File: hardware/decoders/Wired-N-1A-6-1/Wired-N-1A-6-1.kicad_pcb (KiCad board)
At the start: 2 copper layers, 9 x 25 mm, 53 parts, among them J0 CA, J1 CA, J10 RL, J11 RR, J12 FOF, J13 F0R, J14 MCLR, J15 +5, J16 GND, J17 PGD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

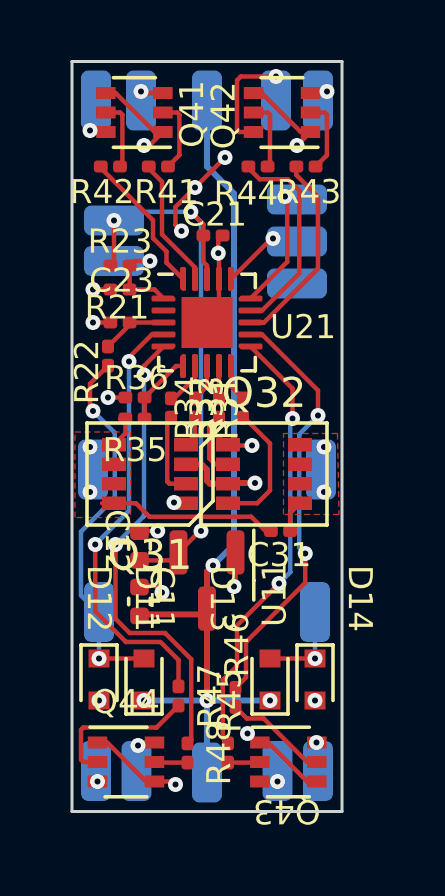
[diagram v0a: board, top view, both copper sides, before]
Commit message: Made Wired-N-1A-6-1 prettier, and easier to follow.
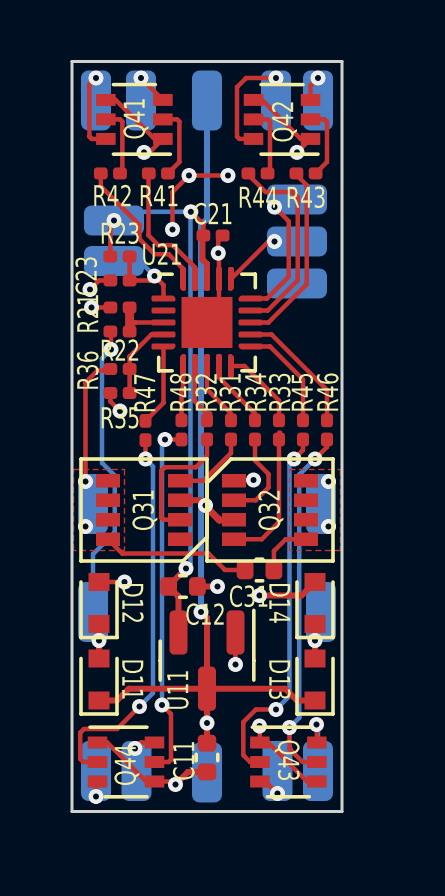
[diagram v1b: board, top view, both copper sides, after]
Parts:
- C11, C12: value 1uF -> 2.2uF
- C31: footprint Capacitor_SMD:C_0201_0603Metric -> Capacitor_SMD:C_0402_1005Metric
- U11: value LR8341A-T50 -> LR8341A
- U21: value PIC18F06Q40 -> PIC18F
- moved R45 11.1 mm to (57.7, 62.3)
- moved R48 10.8 mm to (53.6, 62.3)
- moved R46 9.43 mm to (58.5, 62.3)
- moved R47 8.92 mm to (52.5, 62.3)
- moved C11 5.67 mm to (54.5, 73.2), turned to -90 degrees
- moved U11 2.67 mm to (54.5, 70.0)
- moved D12 2.55 mm to (50.9, 68.0), turned to 90 degrees
- moved D14 2.55 mm to (58.1, 68.0), turned to 90 degrees
- moved C12 1.98 mm to (53.7, 67.5), turned to 0 degrees
- moved R35 1.72 mm to (51.6, 60.2)
- moved D11 1.50 mm to (50.9, 70.6)
- moved D13 1.50 mm to (58.1, 70.6)
- moved C31 1.48 mm to (56.2, 67.0)
- moved R32 1.40 mm to (54.5, 62.3)
- moved R34 1.40 mm to (56.1, 62.3)
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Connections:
- U21 pad 4: F6 -> BackEMF
- U21 pad 5: F0R -> F6
- U21 pad 6: BackEMF -> F0R
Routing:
- net F0R: track 15.7 -> 1.60 mm, vias 2 -> 0
- net F6: track 14.7 -> 2.73 mm, vias 2 -> 0
- net F4: track 14.9 -> 3.34 mm, vias 2 -> 0
- net Net-(Q43-Pad2): track 1.07 -> 12.4 mm, vias 0 -> 2
- net Net-(Q44-Pad5): track 1.11 -> 12.1 mm, vias 0 -> 2
- net F5: track 14.2 -> 4.10 mm, vias 2 -> 0
- net Net-(Q43-Pad5): track 3.47 -> 11.9 mm, vias 0 -> 2
- net Net-(Q44-Pad2): track 5.16 -> 13.0 mm, vias 0 -> 2
- net GND: track 24.1 -> 27.3 mm, vias 18 -> 16
- net FOF_SP: track 0.00 -> 2.63 mm
- net F4_SP: track 0.00 -> 2.18 mm
- net MOT_A: track 7.23 -> 9.29 mm
- net Net-(Q31-Pad2): track 2.84 -> 4.49 mm
- net Net-(Q31-Pad4): track 1.03 -> 2.53 mm
- net +5V: track 19.9 -> 21.2 mm
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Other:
- board text added: "Wired-N-1A-6-1"

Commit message: Bring inline with Breadboard-1 reference design.
Add digital transitor drivers for the high side of the H-Bridge.
Add third BEMF resistor.
Relocate noise capacitor.
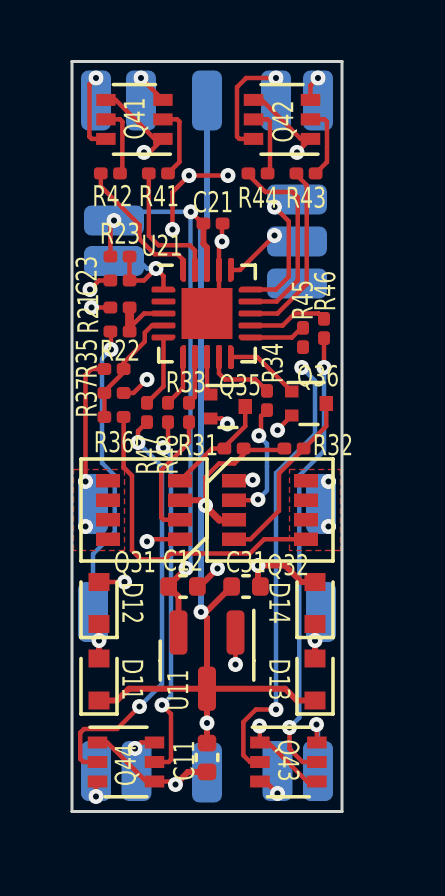
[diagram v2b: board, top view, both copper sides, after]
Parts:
- added Q35: DTC143Z, Package_TO_SOT_SMD:SOT-723, F.Cu at (55.2, 61.5)
- added Q36: DTC143Z, Package_TO_SOT_SMD:SOT-723, F.Cu at (57.9, 61.4)
- added R36: 6K6, Resistor_SMD:R_0201_0603Metric, F.Cu at (51.4, 61.8)
- R31: value 220 -> 10K
- R32: renamed from R33; value 220 -> 10K
- moved R46 3.38 mm to (58.4, 58.9)
- moved R45 3.08 mm to (57.7, 59.2)
- moved R34 1.06 mm to (56.5, 61.3)
- moved R33 0.83 mm to (53.9, 61.7)
- moved R32 0.80 mm to (57.4, 62.9), turned to 180 degrees
- moved R48 0.73 mm to (53.2, 61.7)
- moved C31 0.71 mm to (55.8, 67.5), turned to 180 degrees
- moved R31 0.63 mm to (55.4, 62.9), turned to 180 degrees
- moved R47 0.60 mm to (52.5, 61.7)
- moved C21 0.40 mm to (54.7, 55.4)
- moved U21 0.30 mm to (54.5, 58.4)
- moved R35 0.20 mm to (51.4, 60.2)
- moved R37 0.20 mm to (51.4, 61.0), turned to 180 degrees
- renumbered R32 to R33, R36 to R37
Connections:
- C31 pad 1: MOT_A -> GND
- C31 pad 2: MOT_B -> Vdrive
- R31 pad 1: P1A -> Vdrive
- R32 pad 2: P1C -> Vdrive
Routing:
- net MOT_B: track 1.86 -> 10.8 mm
- net Vdrive: track 33.8 -> 39.3 mm
- net MOT_A: track 9.29 -> 4.26 mm
- net GND: track 27.3 -> 31.1 mm, vias 16 -> 19
- net Net-(Q43-Pad5): track 11.9 -> 15.3 mm
- net Net-(Q43-Pad2): track 12.4 -> 15.2 mm
- net Net-(R32-Pad1): track 4.53 -> 6.12 mm
- net BackEMF: track 2.70 -> 4.23 mm
- net F4: track 3.34 -> 1.88 mm
- net F5: track 4.10 -> 2.69 mm
- net Net-(Q35-Pad3): track 2.53 -> 3.61 mm
- net Net-(Q44-Pad2): track 13.0 -> 14.1 mm
- net Net-(Q32-Pad2): track 3.11 -> 4.14 mm, vias 0 -> 2
- net P1A: track 1.91 -> 1.30 mm
